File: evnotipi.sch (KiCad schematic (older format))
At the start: 23 parts, among them J1 Conn_01x04, J2 Conn_01x03, U1 LM393, U2 LM393

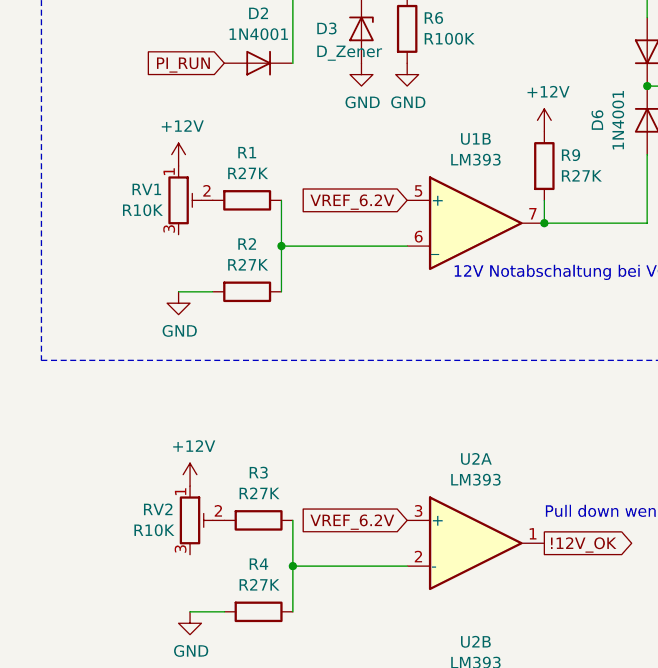
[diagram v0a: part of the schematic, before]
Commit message: Fine adjust voltage splitter
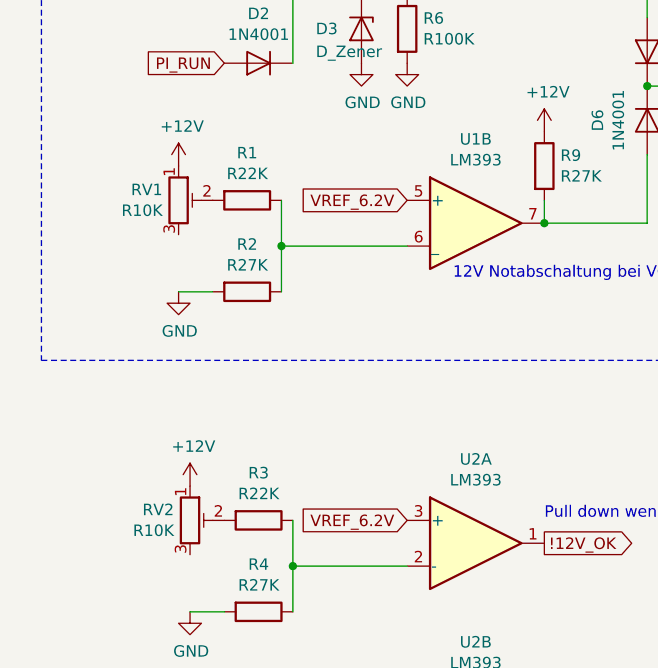
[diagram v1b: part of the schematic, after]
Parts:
- R1, R3: value R27K -> R22K
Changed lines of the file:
@@
 P 1500 3600
 F 0 "R1" V 1293 3600 50  0000 C CNN
-F 1 "R27K" V 1384 3600 50  0000 C CNN
+F 1 "R22K" V 1384 3600 50  0000 C CNN
 F 2 "Resistor_THT:R_Axial_DIN0207_L6.3mm_D2.5mm_P7.62mm_Horizontal" V 1430 3600 50  0001 C CNN
 F 3 "~" H 1500 3600 50  0001 C CNN
@@
 P 1550 5000
 F 0 "R3" V 1343 5000 50  0000 C CNN
-F 1 "R27K" V 1434 5000 50  0000 C CNN
+F 1 "R22K" V 1434 5000 50  0000 C CNN
 F 2 "Resistor_THT:R_Axial_DIN0207_L6.3mm_D2.5mm_P7.62mm_Horizontal" V 1480 5000 50  0001 C CNN
 F 3 "~" H 1550 5000 50  0001 C CNN
